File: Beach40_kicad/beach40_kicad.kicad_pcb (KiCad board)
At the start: 2 copper layers, 200 x 100 mm, 80 parts, among them P1 LO In, P2 MIC_IN, P3 Audio Out, P4 ANT, Q1 BC548, Q2 2N2222, Q3 BD139, Q4 BD139, Q5 BC548, T1 4:10_Transformer, U1 LM386

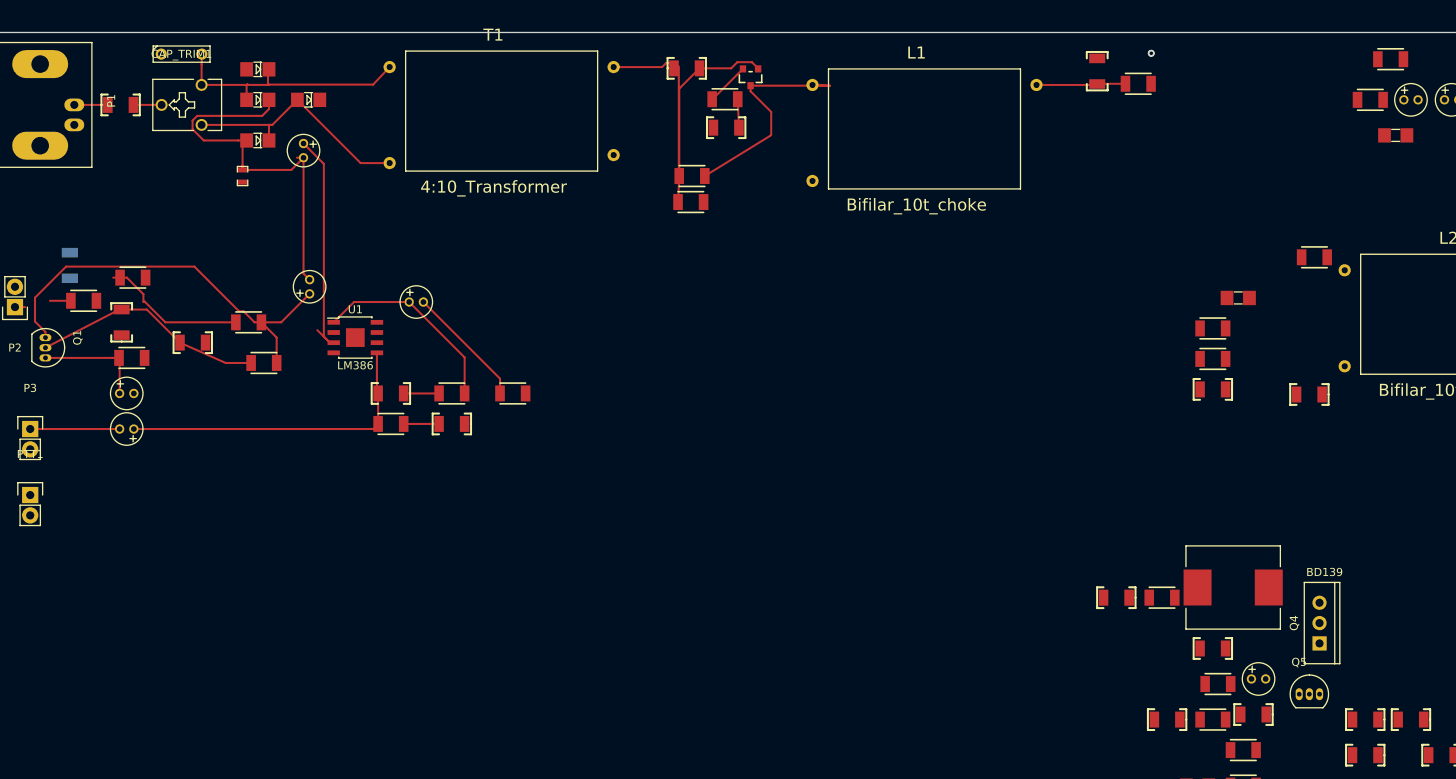
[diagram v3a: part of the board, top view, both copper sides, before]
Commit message: - a mistake or two in the schematic! - just noticed the relay is not correct, pin mappings wierd, custom part time! - more layout
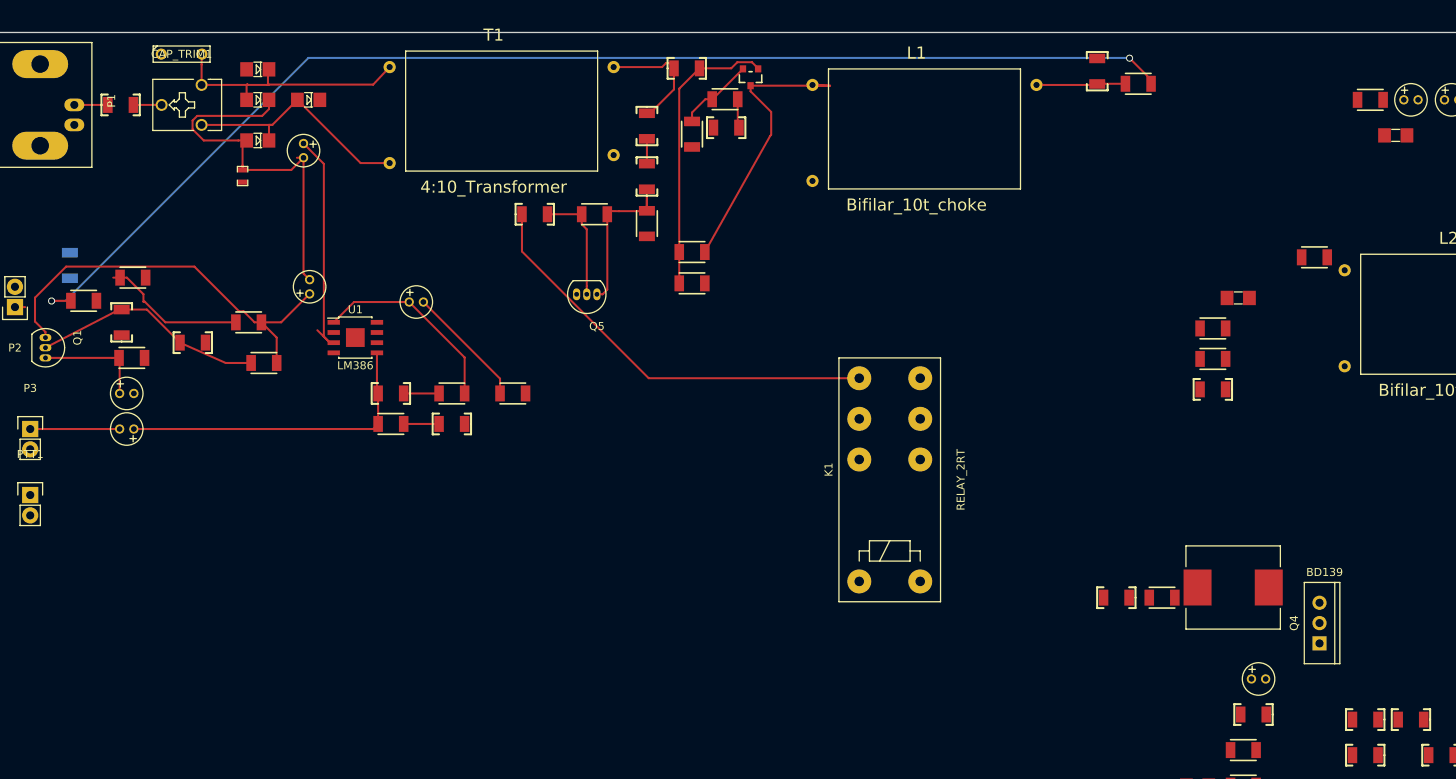
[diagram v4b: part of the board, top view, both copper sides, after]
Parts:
- added K1: RELAY_2RT, Relays_ThroughHole:Relay_DPDT_Schrack-RT2_RM5mm, F.Cu at (166.6, 118.6)
- moved C31 101.2 mm to (118.4, 72.7), turned to 180 degrees
- moved Q5 101.0 mm to (126.2, 82.7), turned to 180 degrees
- moved R21 99.8 mm to (125.9, 72.7), turned to 180 degrees
- moved C33 92.1 mm to (132.5, 68.0), turned to 270 degrees
- moved R22 91.7 mm to (132.5, 73.9), turned to 90 degrees
- moved C15 89.3 mm to (132.5, 61.7), turned to 90 degrees
- moved R12 87.8 mm to (138.1, 62.7), turned to 270 degrees
- moved R11 10.2 mm to (138.1, 81.4)
- moved R10 9.50 mm to (138.1, 77.4)
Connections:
- C26 pad 1: T/R-P-NC -> T/R-P-NO
- L9 pad 2: T/R-P-NC -> T/R-P-NO
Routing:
- net T/R-P-NO: track 2.62 -> 154.1 mm, vias 0 -> 2
- net T/R-S-NC: track 0.00 -> 53.4 mm
- net Net-(C33-Pad2): track 0.00 -> 20.8 mm
- net Net-(C31-Pad1): track 0.00 -> 14.5 mm
- net Net-(C15-Pad2): track 8.09 -> 15.3 mm
- net Net-(L1-Pad1): track 29.1 -> 36.2 mm
- net Net-(Q2-PadE): track 5.42 -> 9.73 mm
- net Net-(C16-Pad1): track 39.6 -> 36.0 mm
- net Net-(C15-Pad1): track 0.00 -> 3.10 mm
- net (no net): track 0.29 -> 0.00 mm, vias 1 -> 0

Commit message: random update, don't remember, think it was mucking about with vias
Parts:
- moved C32 69.5 mm to (212.2, 65.9), turned to 180 degrees
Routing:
- net T/R-P-NC: track 0.00 -> 193.3 mm

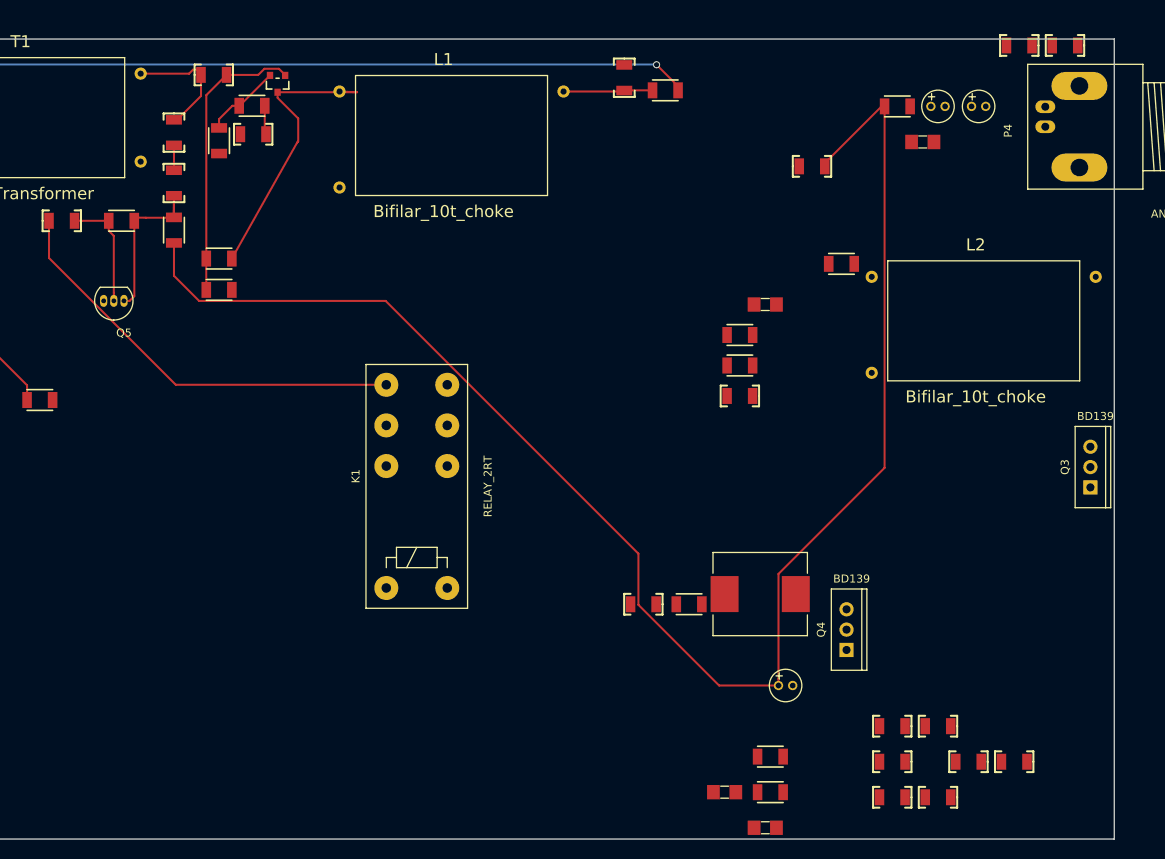
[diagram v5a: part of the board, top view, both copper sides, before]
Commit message: new relay footprint that matches the schematic some more layout, RF path not good though.
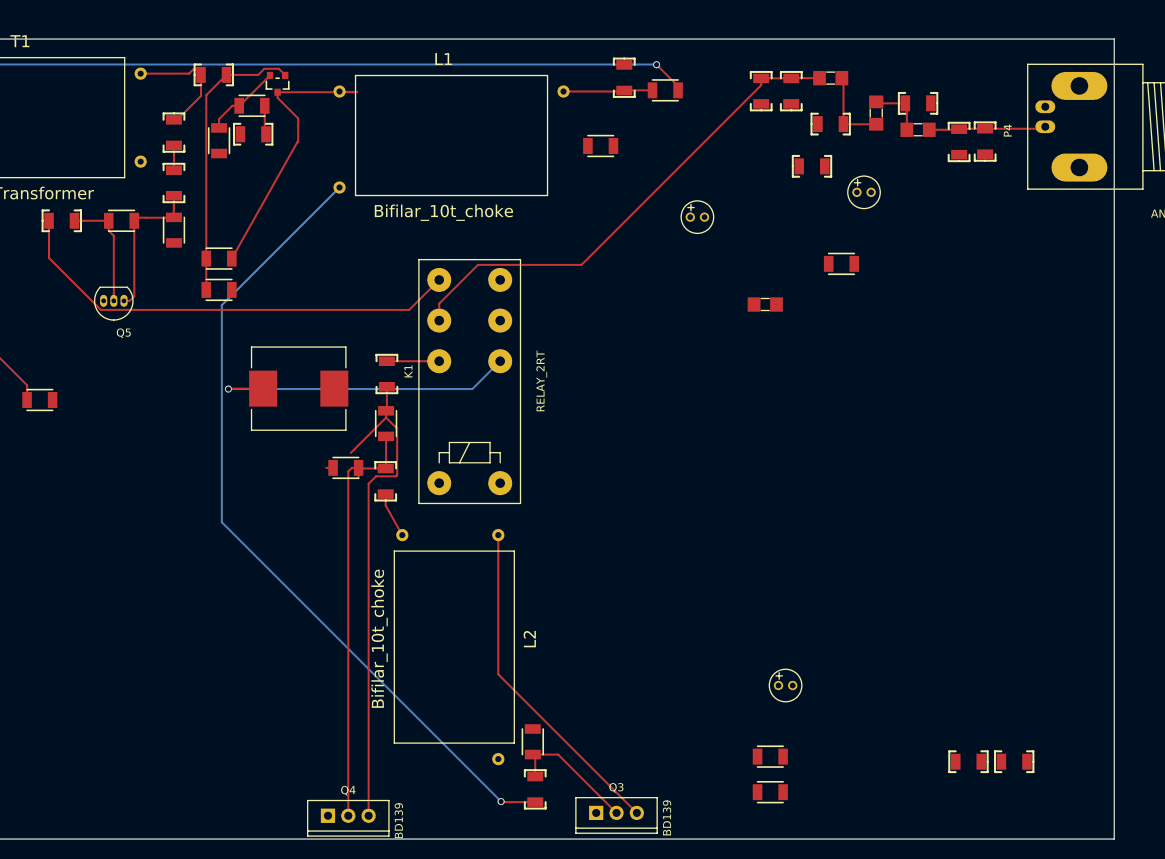
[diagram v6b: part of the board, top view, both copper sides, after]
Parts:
- K1: footprint Relays_ThroughHole:Relay_DPDT_Schrack-RT2_RM5mm -> custom_relay:Relay_DPDT_Custom
- moved L6 90.4 mm to (220.2, 59.3), turned to 90 degrees
- moved L3 90.2 mm to (214.6, 54.9)
- moved C24 86.8 mm to (225.5, 58.0)
- moved C18 85.4 mm to (205.9, 56.5), turned to 270 degrees
- moved C22 85.2 mm to (214.6, 60.6), turned to 180 degrees
- moved C19 80.4 mm to (209.6, 56.5), turned to 270 degrees
- moved L2 77.9 mm to (167.0, 126.0), turned to 270 degrees
- moved Q3 73.3 mm to (187.8, 146.7), turned to 270 degrees
- moved Q4 66.5 mm to (154.3, 147.1), turned to 270 degrees
- moved L9 63.1 mm to (148.1, 93.7), turned to 180 degrees
- moved R14 57.1 mm to (177.3, 137.8), turned to 90 degrees
- moved C20 51.0 mm to (177.6, 143.8), turned to 90 degrees
- moved R19 50.9 mm to (153.9, 103.6), turned to 180 degrees
- moved C25 45.5 mm to (158.9, 105.3), turned to 270 degrees
- moved R18 44.1 mm to (159.0, 98.1), turned to 270 degrees
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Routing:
- net T/R-P-NC: track 193.3 -> 0.40 mm
- net Net-(C20-Pad1): track 0.00 -> 101.6 mm, vias 0 -> 1
- net Net-(C29-Pad2): track 0.00 -> 63.4 mm
- net LPF: track 0.00 -> 61.8 mm
- net Net-(C25-Pad1): track 0.00 -> 53.2 mm
- net Net-(L2-Pad1): track 0.00 -> 41.9 mm
- net T/R-P-NO: track 154.1 -> 193.9 mm, vias 2 -> 3
- net Net-(C20-Pad2): track 0.00 -> 16.4 mm
- net Net-(C27-Pad1): track 0.00 -> 14.7 mm
- net Net-(C22-Pad1): track 0.00 -> 9.93 mm
- net Net-(C24-Pad1): track 0.00 -> 7.09 mm
- net T/R-S-NO: track 0.00 -> 6.54 mm
- net Net-(C25-Pad2): track 0.00 -> 5.67 mm
- net T/R-S-NC: track 53.4 -> 57.7 mm
- net GND: track 0.00 -> 0.85 mm

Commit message: updates updates updates!
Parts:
- C21, C23, R15, R16, R17: moved to B.Cu
- moved R15 69.1 mm to (189.4, 141.9), turned to 180 degrees
- moved C21 59.5 mm to (178.0, 141.6), turned to 90 degrees
- moved C9 59.1 mm to (215.0, 72.0)
- moved C23 38.0 mm to (193.9, 137.9)
- moved L7 34.0 mm to (180.6, 105.4), turned to 180 degrees
- moved C10 26.5 mm to (192.8, 63.5)
- moved R16 22.3 mm to (186.7, 134.8)
- moved R17 20.4 mm to (186.7, 137.9)
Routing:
- net Net-(Q3-Pad1): track 0.00 -> 12.0 mm
- net T/R-P-NO: track 193.9 -> 199.0 mm
- net Net-(L2-Pad1): track 41.9 -> 47.0 mm
- net Net-(C20-Pad2): track 16.4 -> 21.2 mm
- net Net-(C23-Pad1): track 0.00 -> 4.01 mm
